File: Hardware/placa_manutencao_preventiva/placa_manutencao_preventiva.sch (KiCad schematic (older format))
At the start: 38 parts, among them J1 ENT_DIGITAL, J12 Conn_01x01, J13 Conn_01x01, J14 Conn_01x01, J15 Conn_01x01, J16 Conn_01x01, J17 Conn_01x01, J18 Conn_01x01, J19 Conn_01x01, J2 Power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

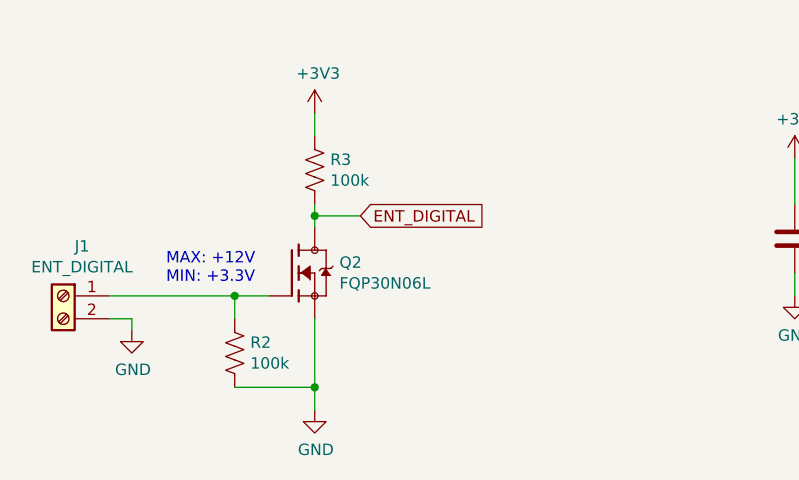
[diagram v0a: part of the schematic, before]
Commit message: Substituição do mosfet para BSS-89
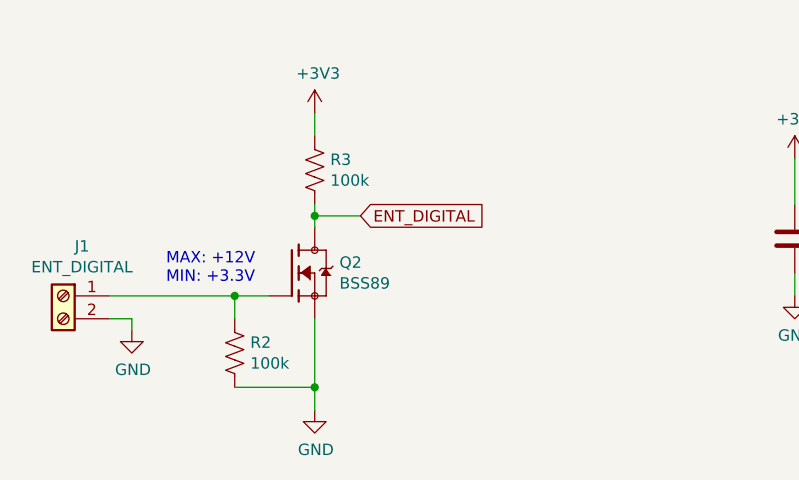
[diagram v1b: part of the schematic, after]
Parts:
- removed Q2: FQP30N06L, fqp30n06l:TO220V, symbol placa_manutencao_preventiva-rescue:FQP30N06L-FQP30N06L
- added Q2: BSS89, TO-92L_Inline, symbol placa_manutencao_preventiva-rescue:BSS89
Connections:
- net ENT_DIGITAL: now also Q2.2 (D)
- net GND: now also Q2.1 (S)
- net at J1.1 (Pin_1), R2.1: now also Q2.3 (G)
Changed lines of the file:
@@
 	1100 7050 1000 7050
-$Comp
-L placa_manutencao_preventiva-rescue:FQP30N06L-FQP30N06L Q2
-U 1 1 5F9A92EB
-P 1800 6850
-F 0 "Q2" H 2008 6896 50  0000 L CNN
-F 1 "FQP30N06L" H 2008 6805 50  0000 L CNN
-F 2 "fqp30n06l:TO220V" H 1800 6850 50  0001 L BNN
-F 3 "" H 1800 6850 50  0001 C CNN
-	1    1800 6850
-	1    0    0    -1
-$EndComp
 $Comp
 L Device:R_US R2
@@
 Wire Wire Line
 	8300 3500 7900 3500
+$Comp
+L placa_manutencao_preventiva-rescue:BSS89 Q2
+U 1 1 605CA543
+P 1800 6850
+F 0 "Q2" H 2008 6896 50  0000 L CNN
+F 1 "BSS89" H 2008 6805 50  0000 L CNN
+F 2 "TO-92L_Inline" H 1800 6850 50  0001 L BNN
+F 3 "" H 1800 6850 50  0001 C CNN
+	1    1800 6850
+	1    0    0    -1
+$EndComp
 $EndSCHEMATC
